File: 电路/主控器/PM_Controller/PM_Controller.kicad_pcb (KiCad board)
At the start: 4 copper layers, 90 x 61.5 mm, 132 parts, among them J1 Conn_01x04_Socket, J10 Conn_02x04_Odd_Even, J11 Conn_02x06_Odd_Even, J2 Conn_01x04_Socket, J3 Conn_01x04_Socket, J4 Conn_01x04_Socket, J5 Conn_01x02_Pin, J6 Conn_01x02_Pin, J7 Conn_02x04_Odd_Even, J8 Conn_01x04_Pin, J9 Conn_01x04_Socket, P3V3 SolderJumper_2_Open, Q2 AO3400A, Q3 AO3400A, Q5 AO3400A, Q6 AO3400A, U1 AT24CS08-SSHM, U10 TMP102xxDRL, U11 TPS2552DDBVR, U12 TLP127, U13 TLV61048DBVR, U2 AMS1117-3.3, U3 STM32G431RBTx, U5 BQ21040DBV, U6 TPS2552DDBVR, U7 STM32L011D4Px, U8 ME6211C25M5, U9 AT24CS08-SSHM, Y1 32.768kHz, Y2 24Mhz

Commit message: 保存主控 Rev2.0 开发快照并更新 Rev3 对焦结构
整理对焦组件目录和依赖，保留 Rev1.3 历史资料，更新结构与 PCB 兼容性说明；排除本地锁文件、调试日志和自动备份。
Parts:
- removed BT1: Battery_Cell, KiCadLib:cr1220
- removed C17, C18, C19, C20: 22uf, Capacitor_SMD:C_0603_1608Metric_Pad1.08x0.95mm_HandSolder
- removed C21, C23, C26, C28, C29, C30, C31, C33, C36, C37, C7: 100nf, Capacitor_SMD:C_0603_1608Metric_Pad1.08x0.95mm_HandSolder
- removed C22, C27, C8: 10uf, Capacitor_SMD:C_0603_1608Metric_Pad1.08x0.95mm_HandSolder
- removed C24: 47uf, Capacitor_Tantalum_SMD:CP_EIA-3528-21_Kemet-B_Pad1.50x2.35mm_HandSolder
- removed C25: 5pf, Capacitor_SMD:C_0603_1608Metric_Pad1.08x0.95mm_HandSolder
- removed C32, C34, C35: 1uf, Capacitor_SMD:C_0603_1608Metric_Pad1.08x0.95mm_HandSolder
- removed C38, C5, C6: 22uf, Capacitor_Tantalum_SMD:CP_EIA-3528-21_Kemet-B_Pad1.50x2.35mm_HandSolder
- removed C39: 22uf, Capacitor_Tantalum_SMD:CP_EIA-3528-21_Kemet-B_HandSolder
- removed C4: 100nf, Capacitor_SMD:C_0603_1608Metric
- removed C40: 1uf, Capacitor_SMD:C_1206_3216Metric_Pad1.33x1.80mm_HandSolder
- removed C41: 10uf, Capacitor_SMD:C_1206_3216Metric_Pad1.33x1.80mm_HandSolder
- removed CHG1, PW_LED1: LED, LED_SMD:LED_0805_2012Metric_Pad1.15x1.40mm_HandSolder
- removed D1: SS34, Diode_SMD:D_SMA
- removed D3: SS32, Diode_SMD:D_SMA_Handsoldering
- removed D4: 1N5819WS, Diode_SMD:D_SOD-323_HandSoldering
- removed FB1: FerriteBead, Inductor_SMD:L_0805_2012Metric_Pad1.05x1.20mm_HandSolder
- removed FLASH1: Conn_01x02_Pin, Connector_Wire:SolderWire-0.1sqmm_1x02_P3.6mm_D0.4mm_OD1mm_Relief
- removed H1, H2, H3, H4: MountingHole, MountingHole:MountingHole_3.2mm_M3
- removed H5, H6, H7, H8, H9: MountingHole_Pad, MountingHole:MountingHole_3.2mm_M3_DIN965_Pad_TopBottom
- removed J1, J4: Conn_01x04_Socket, Connector_JST:JST_PH_S4B-PH-K_1x04_P2.00mm_Horizontal
- removed J10, J7: Conn_02x04_Odd_Even, Connector_PinHeader_1.27mm:PinHeader_2x04_P1.27mm_Vertical
- removed J11: Conn_02x06_Odd_Even, Connector_PinHeader_1.27mm:PinHeader_2x06_P1.27mm_Vertical
- removed J2, J3, J9: Conn_01x04_Socket, Connector_PinHeader_2.54mm:PinHeader_1x04_P2.54mm_Vertical
- removed J5: Conn_01x02_Pin, Connector_Wire:SolderWire-0.5sqmm_1x02_P4.8mm_D0.9mm_OD2.3mm
- removed J6: Conn_01x02_Pin, Connector_PinSocket_2.00mm:PinSocket_1x02_P2.00mm_Vertical
- removed J8: Conn_01x04_Pin, Connector_PinHeader_2.00mm:PinHeader_1x04_P2.00mm_Vertical
- removed JP1, JP2: SolderJumper_3_Bridged12, Jumper:SolderJumper-3_P1.3mm_Bridged12_Pad1.0x1.5mm
- removed L2, L3: 4.7uH, Inductor_SMD:L_APV_APH0650
- removed NRST1, NRST2, P3V3: SolderJumper_2_Open, Jumper:SolderJumper-2_P1.3mm_Open_RoundedPad1.0x1.5mm
- removed Q2, Q3, Q5, Q6: AO3400A, Package_TO_SOT_SMD:SOT-23
- removed R12, R14, R15, R2, R23, R24, R27, R28, R31, R39, R41, R42, R8: 100k, Resistor_SMD:R_0603_1608Metric_Pad0.98x0.95mm_HandSolder
- removed R13: 1.5k, Resistor_SMD:R_0603_1608Metric_Pad0.98x0.95mm_HandSolder
- removed R16, R17, R18, R20, R21, R22: 100k(NC), Resistor_SMD:R_0603_1608Metric_Pad0.98x0.95mm_HandSolder
- removed R25, R26, R32, R40, R6: 1k, Resistor_SMD:R_0603_1608Metric_Pad0.98x0.95mm_HandSolder
- removed R29, R33, R34, R35, R36, R45, R7: 10k, Resistor_SMD:R_0603_1608Metric_Pad0.98x0.95mm_HandSolder
- removed R30, R38, R43: 150k, Resistor_SMD:R_0603_1608Metric_Pad0.98x0.95mm_HandSolder
- removed R37: 22k, Resistor_SMD:R_0603_1608Metric_Pad0.98x0.95mm_HandSolder
- removed R44: 33k, Resistor_SMD:R_0603_1608Metric_Pad0.98x0.95mm_HandSolder
- removed U10: TMP102xxDRL, Package_TO_SOT_SMD:SOT-563
- removed U11, U6: TPS2552DDBVR, KiCadLib:DBV0006A_TEX
- removed U12: TLP127, Package_SO:MFSOP6-4_4.4x3.6mm_P1.27mm
- removed U13: TLV61048DBVR, footprints:SOT-23-6_DBV_TEX
- removed U5: BQ21040DBV, Package_TO_SOT_SMD:SOT-23-6_Handsoldering
- removed U7: STM32L011D4Px, Package_SO:TSSOP-14_4.4x5mm_P0.65mm
- removed U8: ME6211C25M5, Package_TO_SOT_SMD:SOT-23-5_HandSoldering
- removed U9: AT24CS08-SSHM, Package_SO:SOIC-8_3.9x4.9mm_P1.27mm
- removed Y1: 32.768kHz, Crystal:Crystal_C26-LF_D2.1mm_L6.5mm_Horizontal
- removed Y2: 24Mhz, Crystal:Crystal_DS26_D2.0mm_L6.0mm_Horizontal
- added C13: 22uf, Capacitor_SMD:C_0603_1608Metric, F.Cu at (-213.4, 354.4)
- added C9: 10uf, Capacitor_SMD:C_0805_2012Metric, F.Cu at (-209.2, 349.6)
- added U4: TPS563201, Package_TO_SOT_SMD:SOT-23-6, F.Cu at (-208.8, 356.5)
- C1, C2: value 5pf -> 1uf; footprint Capacitor_SMD:C_0603_1608Metric_Pad1.08x0.95mm_HandSolder -> Capacitor_SMD:C_0603_1608Metric; moved to F.Cu
- C10: value 1uf -> 10uf; footprint Capacitor_SMD:C_0603_1608Metric_Pad1.08x0.95mm_HandSolder -> Capacitor_SMD:C_0805_2012Metric
- C11: value 22uf -> 100nf; footprint Capacitor_Tantalum_SMD:CP_EIA-3528-21_Kemet-B_Pad1.50x2.35mm_HandSolder -> Capacitor_SMD:C_0603_1608Metric; moved to F.Cu
- C12: footprint Capacitor_SMD:C_1206_3216Metric_Pad1.33x1.80mm_HandSolder -> Capacitor_SMD:C_0603_1608Metric
- C14: value 47uf -> 22uf; footprint Capacitor_Tantalum_SMD:CP_EIA-3528-21_Kemet-B_Pad1.50x2.35mm_HandSolder -> Capacitor_SMD:C_0603_1608Metric
- C3: value 5pf -> 22uf; footprint Capacitor_SMD:C_0603_1608Metric_Pad1.08x0.95mm_HandSolder -> Capacitor_SMD:C_0805_2012Metric; moved to F.Cu
- L1: value 4.7uH -> 2.2uH; footprint Inductor_SMD:L_APV_APH0650 -> Inductor_SMD:L_Coilcraft_1008HQ_2520Metric
- R1: value 100k -> 10k; footprint Resistor_SMD:R_0603_1608Metric_Pad0.98x0.95mm_HandSolder -> Resistor_SMD:R_0603_1608Metric; moved to F.Cu
- R3: value RPORG(1k) -> 10k; footprint Resistor_SMD:R_0603_1608Metric_Pad0.98x0.95mm_HandSolder -> Resistor_SMD:R_0603_1608Metric; moved to F.Cu
- R4: value 1.5k -> 10k; footprint Resistor_SMD:R_0603_1608Metric_Pad0.98x0.95mm_HandSolder -> Resistor_SMD:R_0603_1608Metric
- R5: value 22k -> 33.2k; footprint Resistor_SMD:R_0603_1608Metric_Pad0.98x0.95mm_HandSolder -> Resistor_SMD:R_0603_1608Metric; moved to F.Cu
- U1: value AT24CS08-SSHM -> ESP32-S3-WROOM-1; footprint Package_SO:SOIC-8_3.9x4.9mm_P1.27mm -> RF_Module:ESP32-S3-WROOM-1
- U2: value AMS1117-3.3 -> STM32G030K8Tx; footprint Package_TO_SOT_SMD:SOT-223-3_TabPin2 -> Package_QFP:LQFP-32_7x7mm_P0.8mm
- U3: value STM32G431RBTx -> PCF85263AT; footprint Package_QFP:LQFP-64_10x10mm_P0.5mm -> Package_SO:SOIC-8_3.9x4.9mm_P1.27mm
- moved C2 381.7 mm to (-198.5, 353.5), turned to 0 degrees
- moved C3 378.3 mm to (-198.3, 350.7), turned to 0 degrees
- moved C1 378.1 mm to (-196.2, 347.9), turned to -90 degrees
- moved U3 377.1 mm to (-171.8, 394.5), turned to 0 degrees
- moved U2 367.1 mm to (-192.9, 376.4)
- moved U1 362.1 mm to (-183.2, 351.8), turned to 0 degrees
- moved C12 361.9 mm to (-213.4, 351.9), turned to 0 degrees
- moved R3 355.9 mm to (-213.4, 359.4), turned to 0 degrees
- moved C14 355.5 mm to (-213.4, 356.9), turned to 0 degrees
- moved C10 349.0 mm to (-209.2, 352.6), turned to 0 degrees
- moved R5 346.4 mm to (-213.4, 364.4), turned to 0 degrees
- moved R4 343.8 mm to (-213.4, 361.9), turned to 0 degrees
- moved R1 337.4 mm to (-194.6, 347.9), turned to 90 degrees
- moved L1 336.6 mm to (-209.0, 361.2), turned to 0 degrees
- moved C11 335.4 mm to (-213.4, 349.4), turned to 0 degrees
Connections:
- net /BAT_OUT renamed Net-(U4-SW)
- C1 pad 1: /LSE+ -> GND
- C1 pad 2: GND -> /ESP_EN
- C10 pad 1: +5VA -> +6V
- C11 pad 2: GND -> Net-(U4-VBST)
- C12 pad 1: +3.3V -> +3V3
- C14 pad 1: +5V -> +3V3
- C2 pad 1: /LSE- -> GND
- C2 pad 2: GND -> +3.3V
- C3 pad 1: /HSE+ -> GND
- C3 pad 2: GND -> +3.3V
- L1 pad 2: Net-(D4-A) -> +3V3
- R1 pad 1: /_C2P1_ -> /ESP_EN
- R1 pad 2: GND -> +3.3V
- R3 pad 2: GND -> +6V
- R4 pad 1: Net-(CHG1-A) -> Net-(U4-VFB)
- R4 pad 2: +BATT -> GND
- R5 pad 1: Net-(U6-ILIM) -> +3V3
- R5 pad 2: GND -> Net-(U4-VFB)
- U1 pad 1: unconnected-(U1-NC-Pad1) -> GND
- U1 pad 2: unconnected-(U1-NC-Pad2) -> +3.3V
- U1 pad 3: Net-(U1-A2) -> /ESP_EN
- U1 pad 4: GND -> unconnected-(U1-IO4-Pad4)
- U1 pad 5: /I2C2_SDA -> unconnected-(U1-IO5-Pad5)
- U1 pad 6: /I2C2_SCL -> unconnected-(U1-IO6-Pad6)
- U1 pad 7: GND -> unconnected-(U1-IO7-Pad7)
- U1 pad 8: +3.3V -> unconnected-(U1-IO15-Pad8)
- U2 pad 1: GND -> unconnected-(U2-PB9-Pad1)
- U2 pad 2: +3.3V -> unconnected-(U2-PC14-Pad2)
- U2 pad 3: Net-(U2-VI) -> unconnected-(U2-PC15-Pad3)
- U3 pad 1: Net-(D3-K) -> unconnected-(U3-OSCI-Pad1)
- U3 pad 3: /LSE+ -> unconnected-(U3-VBAT-Pad3)
- U3 pad 4: /LSE- -> unconnected-(U3-VSS-Pad4)
- U3 pad 5: /HSE+ -> unconnected-(U3-SDA-Pad5)
- U3 pad 6: /HSE- -> unconnected-(U3-SCL-Pad6)
- U3 pad 7: /NRST1 -> unconnected-(U3-~{INTA}-Pad7)
- U3 pad 8: /LPRX1 -> unconnected-(U3-VDD-Pad8)
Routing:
- net GND: track 131.2 -> 0.00 mm, vias 100 -> 0
- net /SHUT_Trig+: track 66.7 -> 0.00 mm, vias 2 -> 0
- net /I2C2_SDA: track 58.1 -> 0.00 mm, vias 4 -> 0
- net /I2C2_SCL: track 57.9 -> 0.00 mm, vias 4 -> 0
- net /PWR_LED: track 53.8 -> 0.00 mm, vias 2 -> 0
- net Net-(CHG1-A): track 52.2 -> 0.00 mm, vias 2 -> 0
- net /#CHRG: track 45.6 -> 0.00 mm, vias 2 -> 0
- net /I2C3_SCL: track 45.1 -> 0.00 mm, vias 2 -> 0
- net /SPI3_SCK: track 44.7 -> 0.00 mm, vias 2 -> 0
- net /TX2: track 44.4 -> 0.00 mm, vias 1 -> 0
- net /I2C3_SDA: track 43.1 -> 0.00 mm, vias 2 -> 0
- net /KEY3: track 43.1 -> 0.00 mm, vias 1 -> 0
- net +3.3V: track 42.5 -> 0.00 mm, vias 28 -> 0
- net /RX2: track 42.3 -> 0.00 mm, vias 1 -> 0
- net /KEY2: track 41.9 -> 0.00 mm, vias 1 -> 0
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- removed copper zone on B.Cu, net +2V5
- removed copper zone on B.Cu, net +3.3V
- removed copper zone on F.Cu, net +3.3V
- removed copper zone on In2.Cu, net +3.3V
- removed copper zone on F.Cu, net +5V
- removed copper zone on F.Cu, net +5VA
- removed copper zone on B.Cu, net +BATT
- removed copper zone on F.Cu, net +BATT
- removed copper zone on In2.Cu, net +BATT
- removed copper zone on F.Cu, net /BAT_OUT2
- removed copper zone on B.Cu, net GND
- removed copper zone on F.Cu, net GND
- removed copper zone on In1.Cu, net GND
- removed copper zone on F.Cu, net Net-(D4-A)
- removed copper zone on F.Cu, net Net-(U2-VI)
- removed copper zone on B.Cu, net Net-(U3-VDDA)
- removed copper zone on B.Cu, net Net-(U4-SW)
- removed copper zone on F.Cu, net Net-(U4-SW)
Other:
- board outline removed
- board text removed: "Controller For PM1"
- board text removed: "EN+"
- board text removed: "GND"
- board text removed: "PWR_SWD"
- board text removed: "Rev1.2"

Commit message: 主控器与CubeMX配置一致
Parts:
- added R12: 1k, Resistor_SMD:R_0603_1608Metric, F.Cu at (118.9, 95.0)
- added R2: 4.7k, Resistor_SMD:R_0603_1608Metric, F.Cu at (118.9, 92.5)
- added U5: DRV8251ADDAR, EasyEDA:SOPOWERPAD-8_L4.9-W3.9-P1.27-LS6.0-TL-EP, F.Cu at (120.8, 88.1)
- added U6: 74HC165, Package_SO:SOIC-16_3.9x9.9mm_P1.27mm, F.Cu at (100.0, 121.0)
- added U7: 74HC165, Package_SO:SOIC-16_3.9x9.9mm_P1.27mm, F.Cu at (113.7, 121.1)
- moved U2 451.3 mm to (136.5, 67.9), turned to -90 degrees
- moved C1 413.9 mm to (101.0, 59.8)
- moved C10 413.9 mm to (88.0, 64.5)
- moved C11 413.9 mm to (83.8, 61.2)
- moved C12 413.9 mm to (83.8, 63.7)
- moved C13 413.9 mm to (83.8, 66.2)
- moved C14 413.9 mm to (83.8, 68.8)
- moved C2 413.9 mm to (98.7, 65.3)
- moved C3 413.9 mm to (98.9, 62.6)
- moved C9 413.9 mm to (88.0, 61.5)
- moved L1 413.9 mm to (88.2, 73.0)
- moved R1 413.9 mm to (102.6, 59.8)
- moved R3 413.9 mm to (83.8, 71.3)
- moved R4 413.9 mm to (83.8, 73.8)
- moved R5 413.9 mm to (83.8, 76.3)
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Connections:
- C12 pad 1: +3V3 -> +3.3V
- C13 pad 1: +3V3 -> +3.3V
- C14 pad 1: +3V3 -> +3.3V
- L1 pad 2: +3V3 -> +3.3V
- R5 pad 1: +3V3 -> +3.3V
- U1 pad 10: unconnected-(U1-IO17-Pad10) -> /ESP_TXD1
- U1 pad 11: unconnected-(U1-IO18-Pad11) -> /ESP_RXD1
- U1 pad 13: unconnected-(U1-USB_D--Pad13) -> /ESP_UD-
- U1 pad 14: unconnected-(U1-USB_D+-Pad14) -> /ESP_UD+
- U1 pad 17: unconnected-(U1-IO9-Pad17) -> /LCD_RES
- U1 pad 18: unconnected-(U1-IO10-Pad18) -> /LCD_DC
- U1 pad 19: unconnected-(U1-IO11-Pad19) -> /LCD_BLK
- U1 pad 20: unconnected-(U1-IO12-Pad20) -> /LCD_MOSI
- U1 pad 21: unconnected-(U1-IO13-Pad21) -> /LCD_CLK
- U1 pad 22: unconnected-(U1-IO14-Pad22) -> /LCD_CS
- U1 pad 31: unconnected-(U1-IO38-Pad31) -> /MASPI_MOSI
- U1 pad 32: unconnected-(U1-IO39-Pad32) -> /MASPI_MISO
- U1 pad 33: unconnected-(U1-IO40-Pad33) -> /MASPI_CLK
- U1 pad 34: unconnected-(U1-IO41-Pad34) -> /MASPI_CS
- U1 pad 36: unconnected-(U1-RXD0-Pad36) -> /ESP_RXD0
- U1 pad 37: unconnected-(U1-TXD0-Pad37) -> /ESP_TXD0
- U1 pad 4: unconnected-(U1-IO4-Pad4) -> /ESP_TXD2
- U1 pad 5: unconnected-(U1-IO5-Pad5) -> /ESP_RXD2
- U2 pad 11: unconnected-(U2-PA4-Pad11) -> /MASPI_CS
- U2 pad 12: unconnected-(U2-PA5-Pad12) -> /MASPI_CLK
- U2 pad 13: unconnected-(U2-PA6-Pad13) -> /MASPI_MISO
- U2 pad 14: unconnected-(U2-PA7-Pad14) -> /MASPI_MOSI
- U2 pad 22: unconnected-(U2-PA9/PA11-Pad22) -> /STM_TXD1
- U2 pad 23: unconnected-(U2-PA10/PA12-Pad23) -> /STM_RXD1
- U2 pad 24: unconnected-(U2-PA13-Pad24) -> /STM_SWDIO
- U2 pad 25: unconnected-(U2-PA14-Pad25) -> /STM_SWCLK
- U2 pad 28: unconnected-(U2-PB4-Pad28) -> /MotorPWM_A
- U2 pad 29: unconnected-(U2-PB5-Pad29) -> /MotorIN2
- U2 pad 4: unconnected-(U2-VDD-Pad4) -> +3.3V
- U2 pad 6: unconnected-(U2-NRST-Pad6) -> /STM_NRST
- U3 pad 4: unconnected-(U3-VSS-Pad4) -> GND

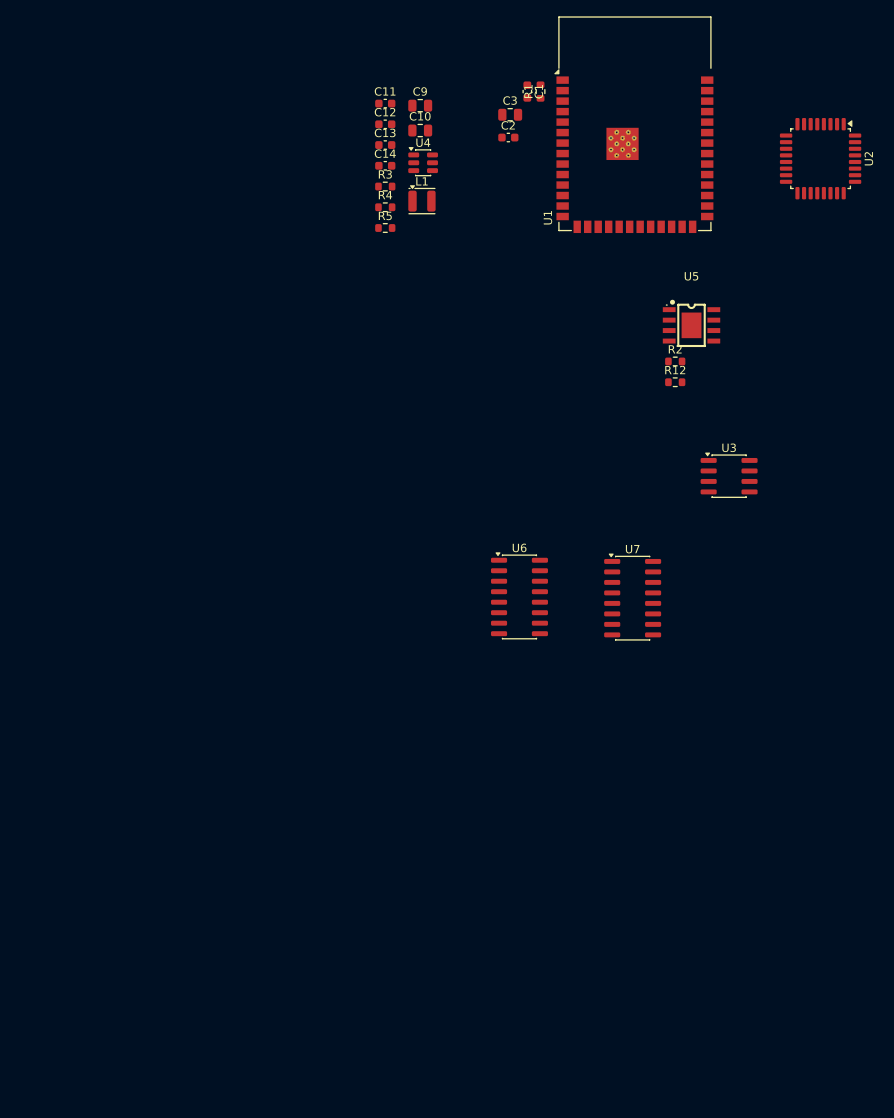
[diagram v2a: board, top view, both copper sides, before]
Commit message: 更新 PM Controller Rev2.0 电路与四层 PCB 设计
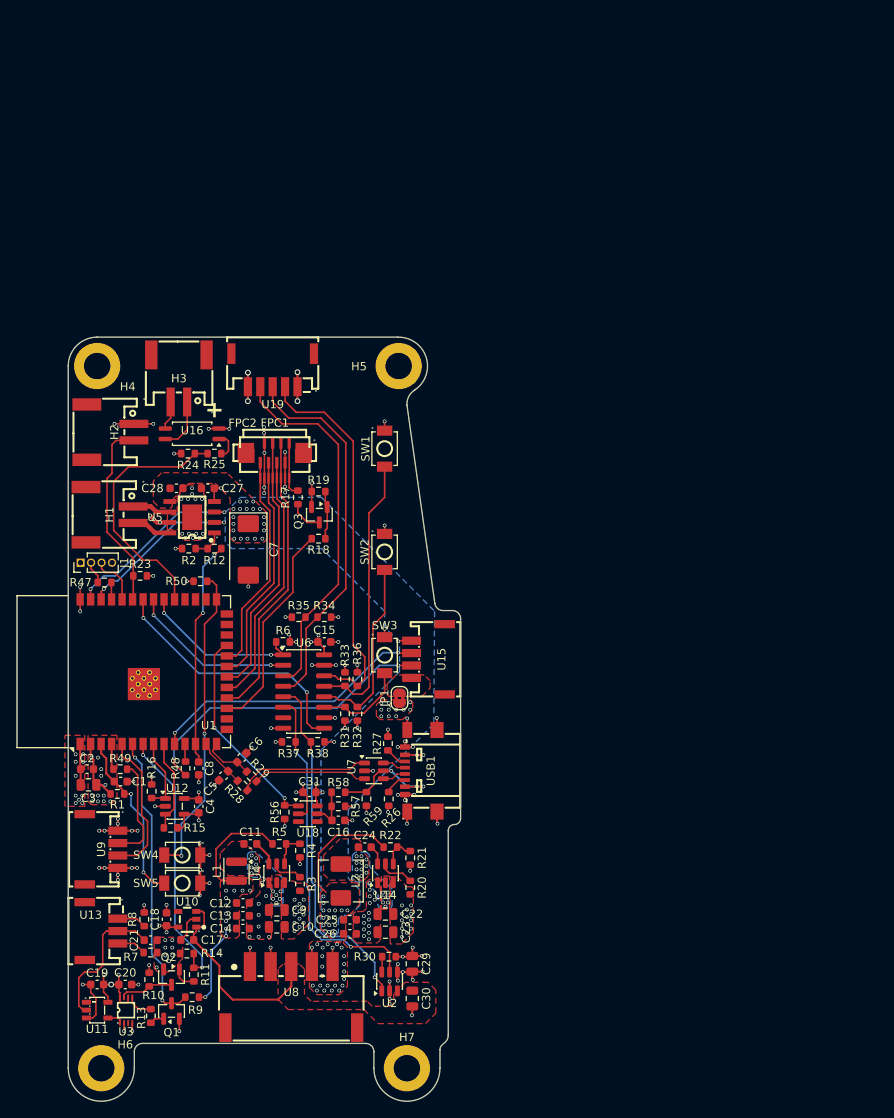
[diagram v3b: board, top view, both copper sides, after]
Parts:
- added C15: 100nF, Capacitor_SMD:C_0603_1608Metric, F.Cu at (76.4, 126.4)
- added C16: 1nf, Capacitor_SMD:C_0603_1608Metric, F.Cu at (78.1, 148.0)
- added C17: 1uf, Capacitor_SMD:C_0603_1608Metric, F.Cu at (59.8, 162.5)
- added C18: 1uf, Capacitor_SMD:C_0603_1608Metric, F.Cu at (57.3, 160.0)
- added C19: 100nf, Capacitor_SMD:C_0603_1608Metric, F.Cu at (48.9, 167.9)
- added C20: 100nf, Capacitor_SMD:C_0603_1608Metric, F.Cu at (52.3, 167.9)
- added C21: 1uf, Capacitor_SMD:C_0603_1608Metric, F.Cu at (55.4, 162.5)
- added C22: 10uf, Capacitor_SMD:C_0805_2012Metric, F.Cu at (83.8, 159.3)
- added C23: 10uf, Capacitor_SMD:C_0805_2012Metric, F.Cu at (83.8, 161.5)
- added C24: 100nf, Capacitor_SMD:C_0603_1608Metric, F.Cu at (81.3, 151.2)
- added C25: 22uf, Capacitor_SMD:C_0603_1608Metric, F.Cu at (79.5, 160.0)
- added C26: 22uf, Capacitor_SMD:C_0603_1608Metric, F.Cu at (79.5, 161.7)
- added C27: 100nF, Capacitor_SMD:C_0603_1608Metric, F.Cu at (62.3, 107.8)
- added C28: 100nf, Capacitor_SMD:C_0603_1608Metric, F.Cu at (58.5, 107.8)
- added C29: 10uf, Capacitor_SMD:C_0805_2012Metric, F.Cu at (87.0, 165.4)
- added C30: 10uf, Capacitor_SMD:C_0805_2012Metric, F.Cu at (87.0, 169.6)
- added C31: 100nF, Capacitor_SMD:C_0603_1608Metric, F.Cu at (74.6, 144.6)
- added C4: 1uf, Capacitor_SMD:C_0603_1608Metric, F.Cu at (61.2, 146.3)
- added C5: DNP, Capacitor_SMD:C_0603_1608Metric, F.Cu at (64.2, 142.6)
- added C6: DNP, Capacitor_SMD:C_0603_1608Metric, F.Cu at (66.4, 140.4)
- added C7: 220uf, Capacitor_Tantalum_SMD:CP_EIA-7343-31_Kemet-D, F.Cu at (67.2, 115.2)
- added C8: TBD(1uf), Capacitor_SMD:C_0603_1608Metric, F.Cu at (61.2, 141.7)
- added FPC1: AFC01-S08FCA-00, EasyEDA:FPC-SMD_P0.50-8P_FGS-XJ-H2.0, F.Cu at (70.4, 105.2)
- added FPC2: AFC11-S08ICA-00, EasyEDA:CONN-TH-8P_AFC11-S08ICA-00, F.Cu at (70.4, 103.5)
- added H1: WAFER-PH2.0-2PWB, EasyEDA:CONN-SMD_2P-P2.00_XUNPU_WAFER-PH2.0-2PWB, F.Cu at (50.4, 111.0)
- added H2: WAFER-PH2.0-2PWB, EasyEDA:CONN-SMD_2P-P2.00_XUNPU_WAFER-PH2.0-2PWB, F.Cu at (50.5, 101.0)
- added H3: WAFER-PH2.0-2PWB, EasyEDA:CONN-SMD_2P-P2.00_XUNPU_WAFER-PH2.0-2PWB, F.Cu at (58.8, 94.5)
- added H4: MountingHole, MountingHole:MountingHole_3.2mm_M3_DIN965_Pad, F.Cu at (48.9, 93.0)
- added H5: MountingHole, MountingHole:MountingHole_3.2mm_M3_DIN965_Pad, F.Cu at (85.4, 93.0)
- added H6: MountingHole, MountingHole:MountingHole_3.2mm_M3_DIN965_Pad, F.Cu at (49.4, 178.0)
- added H7: MountingHole, MountingHole:MountingHole_3.2mm_M3_DIN965_Pad, F.Cu at (86.4, 178.0)
- added J1: Conn_01x04_Pin, Connector_PinHeader_1.27mm:PinHeader_1x04_P1.27mm_Vertical, F.Cu at (46.9, 116.8)
- added JP1: SolderJumper_2_Bridged, Jumper:SolderJumper-2_P1.3mm_Bridged2Bar_RoundedPad1.0x1.5mm, F.Cu at (85.5, 133.2)
- added L2: 3.3uH, Inductor_SMD:L_Changjiang_FXL0530, F.Cu at (78.4, 155.3)
- added Q1: FDV301N, Package_TO_SOT_SMD:SOT-23, F.Cu at (57.9, 171.1)
- added Q2: FDV301N, Package_TO_SOT_SMD:SOT-23, F.Cu at (57.9, 167.0)
- added Q3: SS8550, Package_TO_SOT_SMD:SOT-23, F.Cu at (75.8, 111.0)
- added R10: 10k, Resistor_SMD:R_0603_1608Metric, F.Cu at (55.2, 167.3)
- added R11: 100, Resistor_SMD:R_0603_1608Metric, F.Cu at (60.6, 166.7)
- added R13: 100, Resistor_SMD:R_0603_1608Metric, F.Cu at (55.4, 171.7)
- added R14: 10k, Resistor_SMD:R_0603_1608Metric, F.Cu at (59.8, 164.1)
- added R15: 4.7k, Resistor_SMD:R_0603_1608Metric, F.Cu at (57.8, 148.9)
- added R16: 4.7k, Resistor_SMD:R_0603_1608Metric, F.Cu at (55.5, 144.5)
- added R17: 10, Resistor_SMD:R_0603_1608Metric, F.Cu at (73.2, 108.9)
- added R18: 1k, Resistor_SMD:R_0603_1608Metric, F.Cu at (75.7, 113.9)
- added R19: 10k, Resistor_SMD:R_0603_1608Metric, F.Cu at (75.7, 108.2)
- added R20: 10k, Resistor_SMD:R_0603_1608Metric, F.Cu at (86.8, 156.1)
- added R21: 10k, Resistor_SMD:R_0603_1608Metric, F.Cu at (86.8, 152.5)
- added R22: 68.1k, Resistor_SMD:R_0603_1608Metric, F.Cu at (84.4, 151.2)
- added R23: 10k, Resistor_SMD:R_0603_1608Metric, F.Cu at (54.1, 118.4)
- added R24: 10k, Resistor_SMD:R_0603_1608Metric, F.Cu at (59.9, 103.6)
- added R25: 390, Resistor_SMD:R_0603_1608Metric, F.Cu at (63.1, 103.6)
- added R26: 5.1k, Resistor_SMD:R_0603_1608Metric, F.Cu at (84.2, 145.4)
- added R27: 5.1k, Resistor_SMD:R_0603_1608Metric, F.Cu at (84.1, 138.7)
- added R28: 0, Resistor_SMD:R_0603_1608Metric, F.Cu at (66.5, 143.8)
- added R29: 0, Resistor_SMD:R_0603_1608Metric, F.Cu at (67.6, 142.7)
- added R30: 2.1k (RPROG), Resistor_SMD:R_0603_1608Metric, F.Cu at (84.2, 164.5)
- added R31: 10k, Resistor_SMD:R_0603_1608Metric, F.Cu at (78.9, 135.1)
- added R32: 10k, Resistor_SMD:R_0603_1608Metric, F.Cu at (80.4, 135.1)
- added R33: 10k, Resistor_SMD:R_0603_1608Metric, F.Cu at (78.9, 130.9)
- added R34: 10k, Resistor_SMD:R_0603_1608Metric, F.Cu at (76.4, 123.4)
- added R35: 10k, Resistor_SMD:R_0603_1608Metric, F.Cu at (73.3, 123.4)
- added R36: 10k, Resistor_SMD:R_0603_1608Metric, F.Cu at (80.4, 130.9)
- added R37: 10k, Resistor_SMD:R_0603_1608Metric, F.Cu at (72.1, 138.5)
- added R38: 10k, Resistor_SMD:R_0603_1608Metric, F.Cu at (75.6, 138.5)
- added R47: 499, Resistor_SMD:R_0603_1608Metric, F.Cu at (49.8, 119.2)
- added R48: 499, Resistor_SMD:R_0603_1608Metric, F.Cu at (59.6, 141.7)
- added R49: 499, Resistor_SMD:R_0603_1608Metric, F.Cu at (51.7, 141.8)
- added R50: 10k, Resistor_SMD:R_0603_1608Metric, F.Cu at (61.4, 119.1)
- added R56: 10k, Resistor_SMD:R_0603_1608Metric, F.Cu at (71.6, 147.0)
- added R57: 1k, Resistor_SMD:R_0603_1608Metric, F.Cu at (78.1, 146.3)
- added R58: 10.1k, Resistor_SMD:R_0603_1608Metric, F.Cu at (78.1, 144.6)
- added R59: 680, Resistor_SMD:R_0603_1608Metric, F.Cu at (81.5, 145.4)
- added R6: 10k, Resistor_SMD:R_0603_1608Metric, F.Cu at (71.4, 126.4)
- added R7: 100k, Resistor_SMD:R_0603_1608Metric, F.Cu at (55.3, 164.0)
- added R8: 100k, Resistor_SMD:R_0603_1608Metric, F.Cu at (54.6, 160.0)
- added R9: 10k, Resistor_SMD:R_0603_1608Metric, F.Cu at (60.4, 169.4)
- added SW1: TS-1088R-02026, EasyEDA:SW-SMD_L3.9-W3.0-P4.45, F.Cu at (83.7, 103.0)
- added SW2: TS-1088R-02026, EasyEDA:SW-SMD_L3.9-W3.0-P4.45, F.Cu at (83.7, 115.5)
- added SW3: TS-1088R-02026, EasyEDA:SW-SMD_L3.9-W3.0-P4.45, F.Cu at (83.7, 128.0)
- added SW4: TS-1088R-02026, EasyEDA:SW-SMD_L3.9-W3.0-P4.45, F.Cu at (59.2, 152.2)
- added SW5: TS-1088R-02026, EasyEDA:SW-SMD_L3.9-W3.0-P4.45, F.Cu at (59.2, 155.6)
- added U10: TPS7A0233PDBVR, EasyEDA:SOT-23-5_L2.9-W1.6-P0.95-LS2.8-BR, F.Cu at (59.8, 160.0)
- added U11: SN74AUP1G17DBVR, EasyEDA:SOT-23-5_L3.0-W1.7-P0.95-LS2.8-BR, F.Cu at (48.9, 171.0)
- added U12: 24C64, Package_TO_SOT_SMD:SOT-23-5, F.Cu at (58.3, 146.3)
- added U13: ZX-ZH1.5-3PWT, EasyEDA:CONN-SMD_3P-P1.50_ZX-ZH1.5-3PWT, F.Cu at (49.4, 161.4)
- added U14: TPS563201, Package_TO_SOT_SMD:SOT-23-6, F.Cu at (83.8, 154.4)
- added U15: ZX-ZH1.5-4PWT, EasyEDA:CONN-SMD_4P-P1.50_ZX-ZH1.5-4PWT, F.Cu at (88.9, 128.5)
- added U16: TLP291, Package_SO:SOIC-4_4.55x2.6mm_P1.27mm, F.Cu at (60.4, 101.2)
- added U18: TPS3808G01DBVR, Package_TO_SOT_SMD:SOT-23-6, F.Cu at (74.4, 147.2)
- added U19: ZX-ZH1.5-5PWT, EasyEDA:CONN-SMD_5P-P1.50_ZX-ZH1.5-5PWT, F.Cu at (70.1, 93.5)
- added U8: ZX-XH2.54-5PWT, EasyEDA:CONN-SMD_5P-P2.54_MEGASTAR_ZX-XH2.54-5PWT, F.Cu at (72.4, 169.4)
- added U9: ZX-ZH1.5-4PWT, EasyEDA:CONN-SMD_4P-P1.50_ZX-ZH1.5-4PWT, F.Cu at (49.4, 151.5)
- added USB1: MC-402L68, EasyEDA:USB-C-SMD_MC-402L68, F.Cu at (88.1, 142.0)
- R12: value 1k -> 0
- R2: value 4.7k -> 1k
- U2: value STM32G030K8Tx -> TP4057; footprint Package_QFP:LQFP-32_7x7mm_P0.8mm -> Package_TO_SOT_SMD:TSOT-23-6
- U3: value PCF85263AT -> SN74AUP1G74DCUR; footprint Package_SO:SOIC-8_3.9x4.9mm_P1.27mm -> EasyEDA:VSSOP-8_L2.1-W2.4-P0.50-LS3.2-BR
- U7: value 74HC165 -> USBLC6-2SC6; footprint Package_SO:SOIC-16_3.9x9.9mm_P1.27mm -> Package_TO_SOT_SMD:SOT-23-6
- moved U2 112.4 mm to (84.3, 167.5), turned to 90 degrees
- moved R1 99.3 mm to (51.3, 144.8), turned to 180 degrees
- moved C9 98.9 mm to (70.6, 158.8), turned to 180 degrees
- moved C10 98.0 mm to (70.6, 160.9), turned to 180 degrees
- moved U3 97.5 mm to (52.4, 171.0), turned to -90 degrees
- moved C1 97.0 mm to (51.7, 143.3), turned to 180 degrees
- moved C3 95.8 mm to (47.8, 143.7)
- moved C12 95.8 mm to (66.5, 158.0)
- moved C13 94.9 mm to (66.5, 159.5)
- moved C14 93.9 mm to (66.5, 161.1)
- moved C2 91.9 mm to (47.7, 141.8)
- moved C11 91.1 mm to (67.4, 150.8)
- moved U1 90.7 mm to (52.1, 130.0), turned to 90 degrees
- moved U4 87.8 mm to (70.6, 154.4), turned to 90 degrees
- moved R3 85.1 mm to (73.4, 155.7), turned to -90 degrees
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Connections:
- C10 pad 1: +6V -> VCC
- C9 pad 1: +6V -> VCC
- R3 pad 2: +6V -> VCC
- U1 pad 10: /ESP_TXD1 -> /ESP_RXD2
- U1 pad 11: /ESP_RXD1 -> Net-(U1-IO18)
- U1 pad 12: unconnected-(U1-IO8-Pad12) -> /ADC_MT
- U1 pad 13: /ESP_UD- -> /_1UD-
- U1 pad 14: /ESP_UD+ -> /_1UD+
- U1 pad 17: /LCD_RES -> /LCD_BLK
- U1 pad 18: /LCD_DC -> /LCD_RES
- U1 pad 19: /LCD_BLK -> /LCD_DC
- U1 pad 23: unconnected-(U1-IO21-Pad23) -> /USBPWR_DET
- U1 pad 31: /MASPI_MOSI -> /FLASH_TRG
- U1 pad 32: /MASPI_MISO -> /MASPI_CS
- U1 pad 34: /MASPI_CS -> /MASPI_MISO
- U1 pad 35: unconnected-(U1-IO42-Pad35) -> /SHUT_TRG
- U1 pad 37: /ESP_TXD0 -> Net-(U1-TXD0)
- U1 pad 38: unconnected-(U1-IO2-Pad38) -> /MotorIN2
- U1 pad 39: unconnected-(U1-IO1-Pad39) -> /MotorPWM_A
- U1 pad 4: /ESP_TXD2 -> Net-(U1-IO4)
- U1 pad 5: /ESP_RXD2 -> /ESP_RXD1
- U1 pad 6: unconnected-(U1-IO6-Pad6) -> /ESP_FILM_TRG
- U1 pad 7: unconnected-(U1-IO7-Pad7) -> /ESP_FILM_CLR
- U1 pad 8: unconnected-(U1-IO15-Pad8) -> /ESP_SCL
- U1 pad 9: unconnected-(U1-IO16-Pad9) -> /ESP_SDA
- U2 pad 1: unconnected-(U2-PB9-Pad1) -> /BAT_CHG_OD
- U2 pad 2: unconnected-(U2-PC14-Pad2) -> GND
- U2 pad 3: unconnected-(U2-PC15-Pad3) -> +BATT
- U2 pad 4: +3.3V -> VBUS
- U2 pad 5: GND -> /BAT_STB_OD
- U2 pad 6: /STM_NRST -> Net-(U2-PROG)
- U3 pad 1: unconnected-(U3-OSCI-Pad1) -> Net-(U11-Y)
- U3 pad 2: unconnected-(U3-OSCO-Pad2) -> GND
- U3 pad 5: unconnected-(U3-SDA-Pad5) -> /#FILM_TRG
- U3 pad 6: unconnected-(U3-SCL-Pad6) -> VAA
- U3 pad 7: unconnected-(U3-~{INTA}-Pad7) -> /#FILM_KEY_CLR
- U3 pad 8: unconnected-(U3-VDD-Pad8) -> VAA
- U4 pad 3: +6V -> VCC
- U6 pad 1: unconnected-(U6-~{PL}-Pad1) -> /MASPI_CS
- U6 pad 10: unconnected-(U6-DS-Pad10) -> GND
- U6 pad 11: unconnected-(U6-D0-Pad11) -> /ESP_KEY1
- U6 pad 12: unconnected-(U6-D1-Pad12) -> /ESP_KEY2
- U6 pad 13: unconnected-(U6-D2-Pad13) -> /ESP_KEY3
- U6 pad 14: unconnected-(U6-D3-Pad14) -> /ESP_KEY4
- U6 pad 15: unconnected-(U6-~{CE}-Pad15) -> GND
- U6 pad 2: unconnected-(U6-CP-Pad2) -> /MASPI_CLK
- U6 pad 3: unconnected-(U6-D4-Pad3) -> /ESP_KEY5
- U6 pad 4: unconnected-(U6-D5-Pad4) -> /ESP_KEY6
- U6 pad 5: unconnected-(U6-D6-Pad5) -> /BAT_CHG_OD
- U6 pad 6: unconnected-(U6-D7-Pad6) -> /BAT_STB_OD
- U6 pad 9: unconnected-(U6-Q7-Pad9) -> /MASPI_MISO
- U7 pad 1: unconnected-(U7-~{PL}-Pad1) -> /ESP_UD-
- U7 pad 2: unconnected-(U7-CP-Pad2) -> GND
- U7 pad 3: unconnected-(U7-D4-Pad3) -> /ESP_UD+
- U7 pad 4: unconnected-(U7-D5-Pad4) -> /_UD+
- U7 pad 5: unconnected-(U7-D6-Pad5) -> VBUS
- U7 pad 6: unconnected-(U7-D7-Pad6) -> /_UD-
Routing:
- net GND: track 0.00 -> 114.4 mm, vias 0 -> 153
- net +3.3V: track 0.00 -> 80.1 mm, vias 0 -> 57
- net /ESP_KEY4: track 0.00 -> 47.1 mm
- net /ESP_KEY6: track 0.00 -> 46.1 mm
- net /ESP_KEY5: track 0.00 -> 44.9 mm
- net /BAT_CHG_OD: track 0.00 -> 43.1 mm, vias 0 -> 2
- net /BAT_STB_OD: track 0.00 -> 42.0 mm, vias 0 -> 2
- net /ESP_BOOT: track 0.00 -> 38.0 mm, vias 0 -> 2
- net /ESP_TXD2: track 0.00 -> 37.0 mm, vias 0 -> 2
- net /ESP_FILM_TRG: track 0.00 -> 35.8 mm, vias 0 -> 2
- net /LCD_RES: track 0.00 -> 35.1 mm
- net /ESP_RXD2: track 0.00 -> 34.1 mm, vias 0 -> 2
- net /ESP_KEY3: track 0.00 -> 33.7 mm
- net /ESP_FILM_CLR: track 0.00 -> 32.8 mm, vias 0 -> 2
- net /LCD_MOSI: track 0.00 -> 32.0 mm
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- added copper zone on F.Cu, net +3.3V
- added copper zone on In2.Cu, net +3.3V
- added copper zone on B.Cu, net +6V
- added copper zone on F.Cu, net +6V
- added copper zone on F.Cu, net +BATT
- added copper zone on F.Cu, net GND
- added copper zone on In1.Cu, net GND
- added copper zone on F.Cu, net Net-(JP1-B)
- added copper zone on B.Cu, net Net-(U14-SW)
- added copper zone on F.Cu, net Net-(U14-SW)
- added copper zone on B.Cu, net Net-(U4-SW)
- added copper zone on F.Cu, net Net-(U4-SW)
- added copper zone on In2.Cu, net VAA
- added copper zone on In2.Cu, net VBUS
- added copper zone on F.Cu, net VCC
- added copper zone on In2.Cu, net VCC
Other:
- board outline added: 47.5 x 92.5 mm
- board text added: "+"
